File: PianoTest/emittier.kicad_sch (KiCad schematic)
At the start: 14 parts, among them J301 TRIG est., Q301 BSS138, U301 LTC6993CS6-2, U302 AD5245BRJZ100

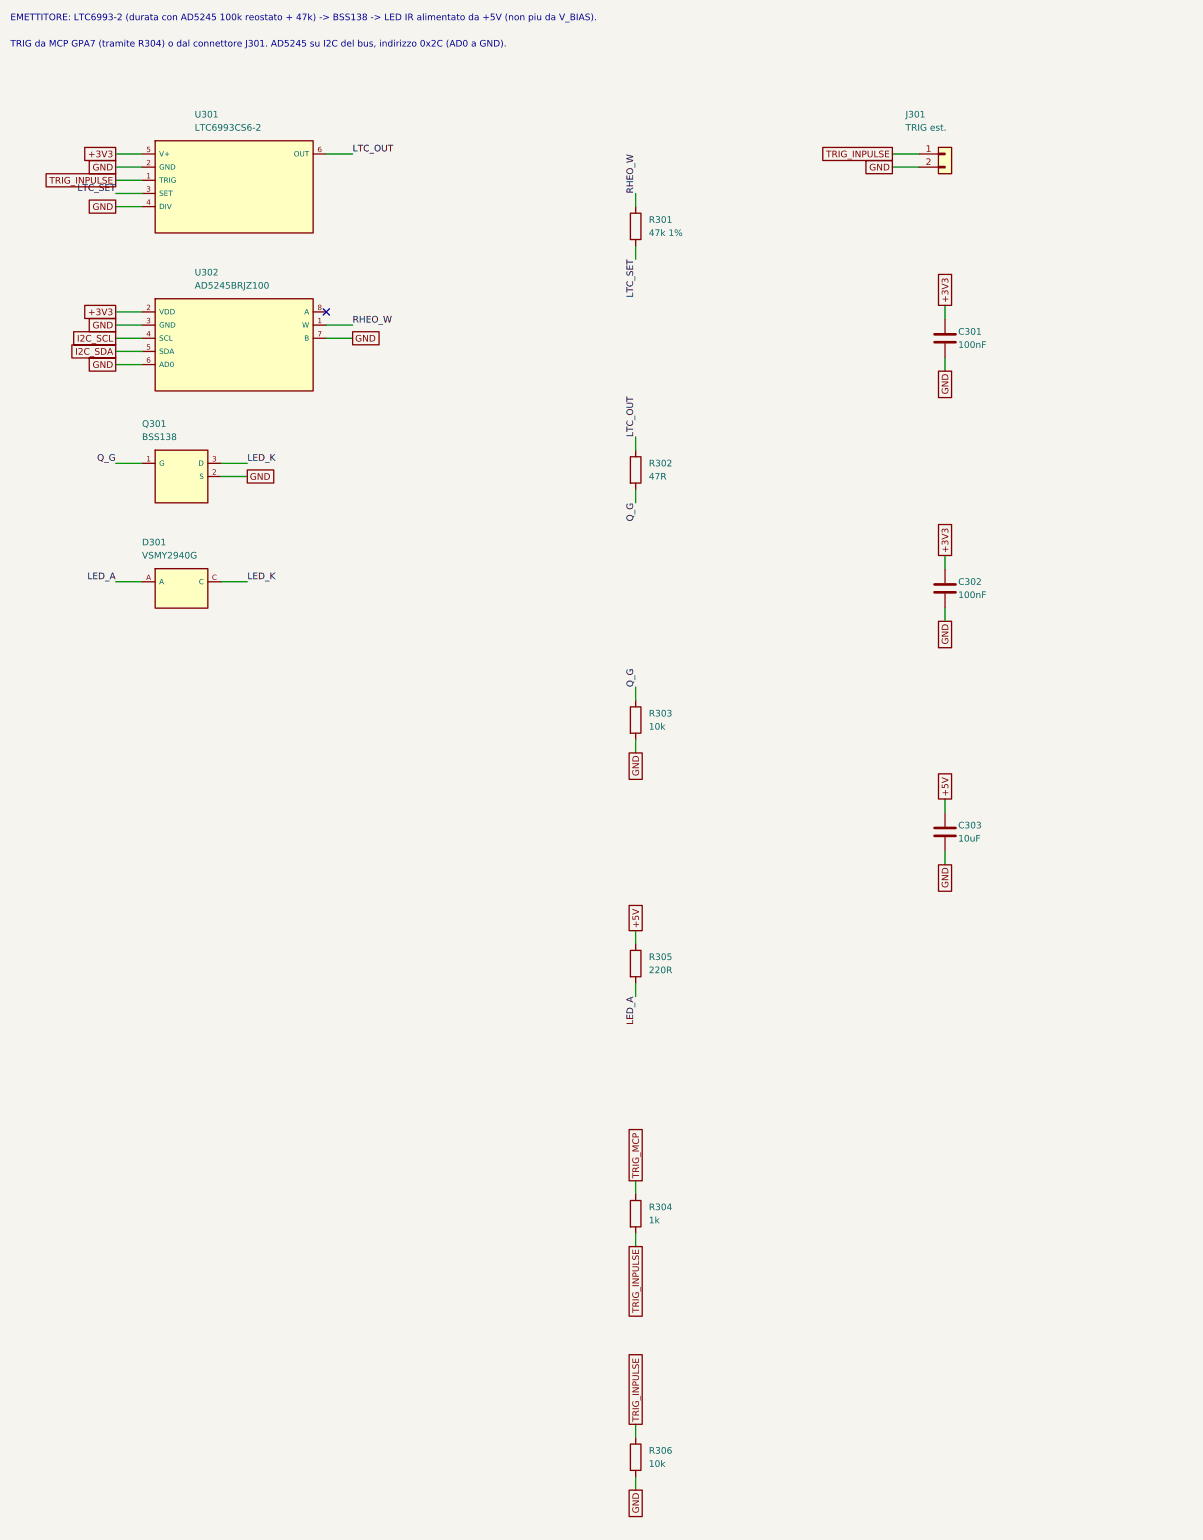
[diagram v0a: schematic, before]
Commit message: PianoTest: discriminatore, latch e rilevatore di picco
Comparatore TLV3501 su SHAPER_OUT con soglia dal canale B del DAC61402
(partitore 22k/10k, BAT54S), latch 74LVC1G74 su GPA7 dell'MCP (ALERT#),
uscita HIT su TP e SMA. Rilevatore di picco OPA2365 + BAS416 + hold 1 nF
C0G prima dell'ADS8326, con reset da accesso SPI all'indirizzo 3 e
ponticello 0R per scavalcarlo. Trigger del LED dallo strobe dell'indirizzo 4.
Articolo: sezione 3.1 (formatore e acquisizione) aggiornata e ricompilata.
ERC 0.

Co-Authored-By: Claude Opus 5.5 (1M context) <noreply@anthropic.com>
Claude-Session: https://claude.ai/code/session_01J3krgWFTUEjwvCnwUp9cQn
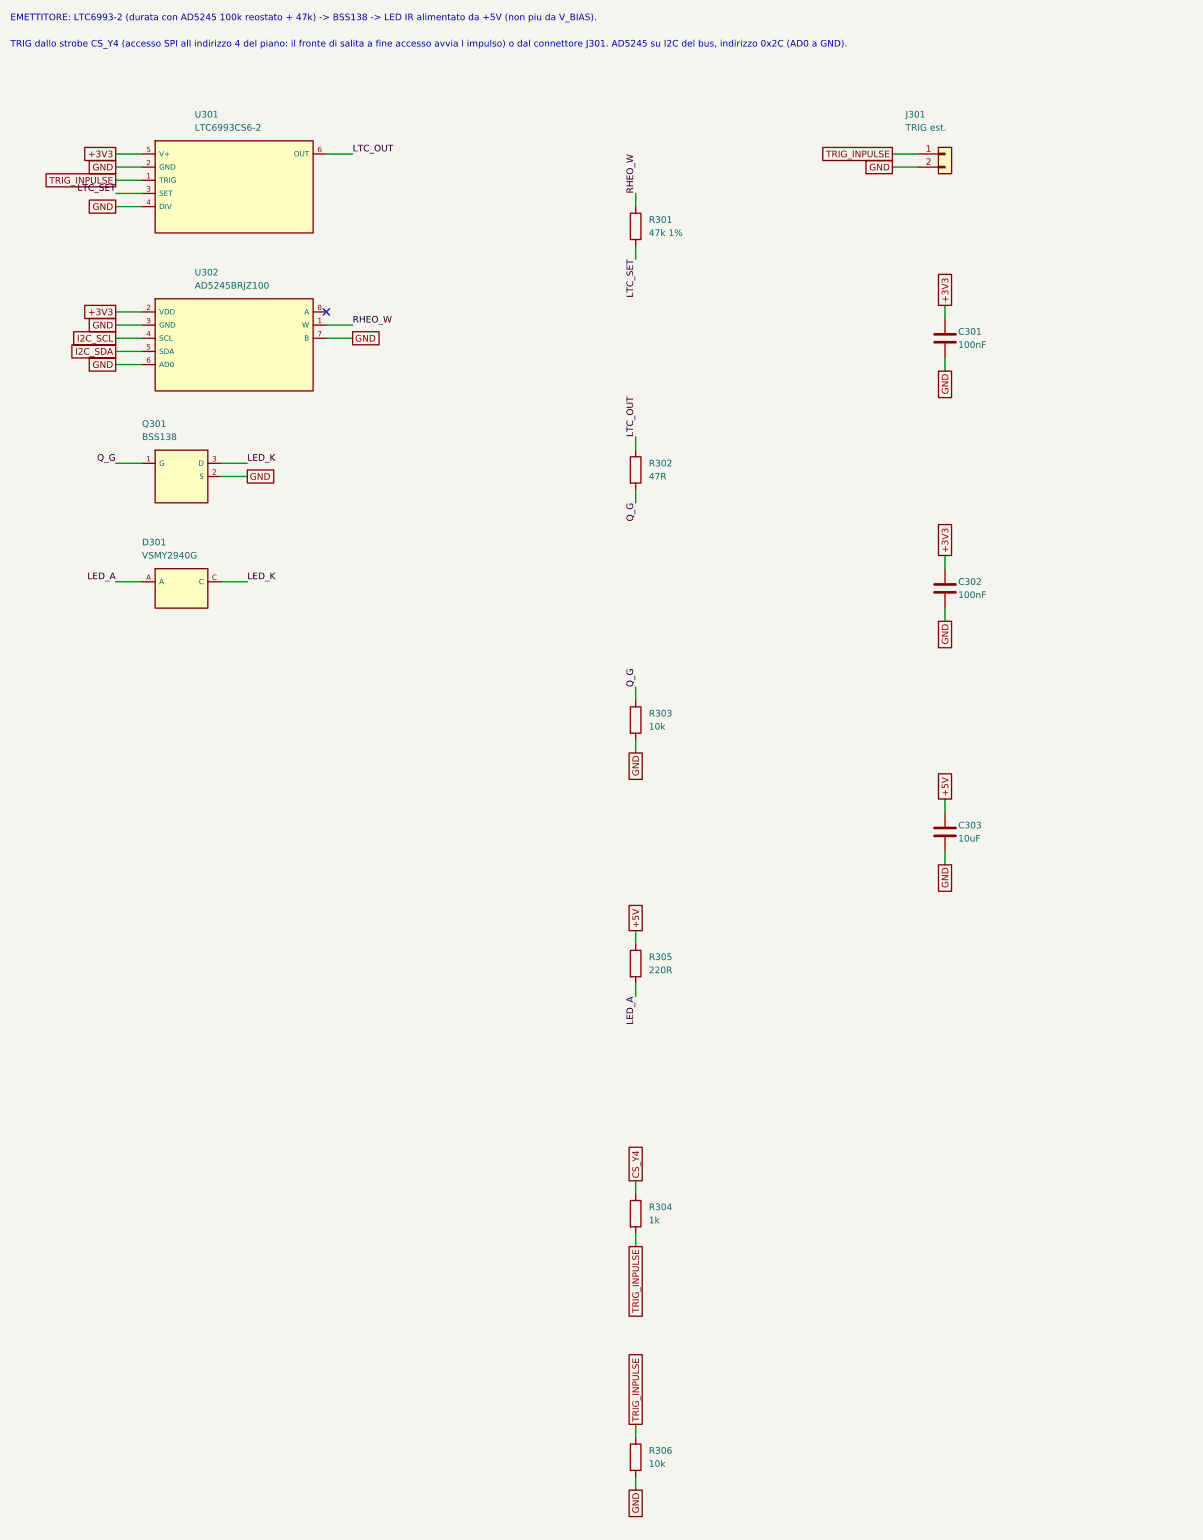
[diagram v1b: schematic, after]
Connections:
- net TRIG_MCP renamed CS_Y4
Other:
- note added: "TRIG dallo strobe CS_Y4 (accesso SPI all indirizzo 4 del piano: il fronte di salita a fine accesso avvia l impulso) o dal connettore J301. AD5245 su I2C del bus, indirizzo 0x2C (AD0 a GND)."
- note removed: "TRIG da MCP GPA7 (tramite R304) o dal connettore J301. AD5245 su I2C del bus, indirizzo 0x2C (AD0 a GND)."
